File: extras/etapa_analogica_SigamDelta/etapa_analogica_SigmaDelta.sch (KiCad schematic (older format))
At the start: 20 parts, among them P1 CONN_02X10, P2 CONN_01X03, P3 CONN_02X10, P4 BNC

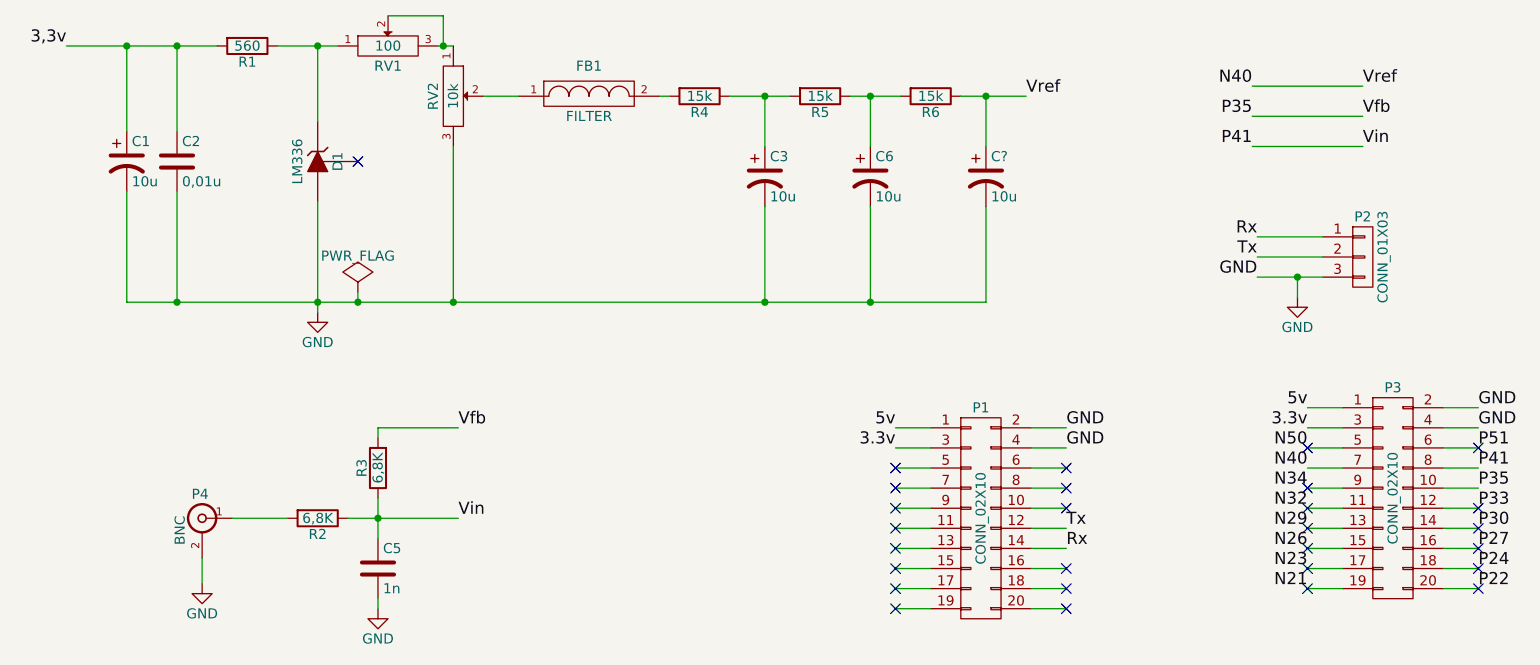
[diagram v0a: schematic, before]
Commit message: Agregado rooteo placa en Kicad
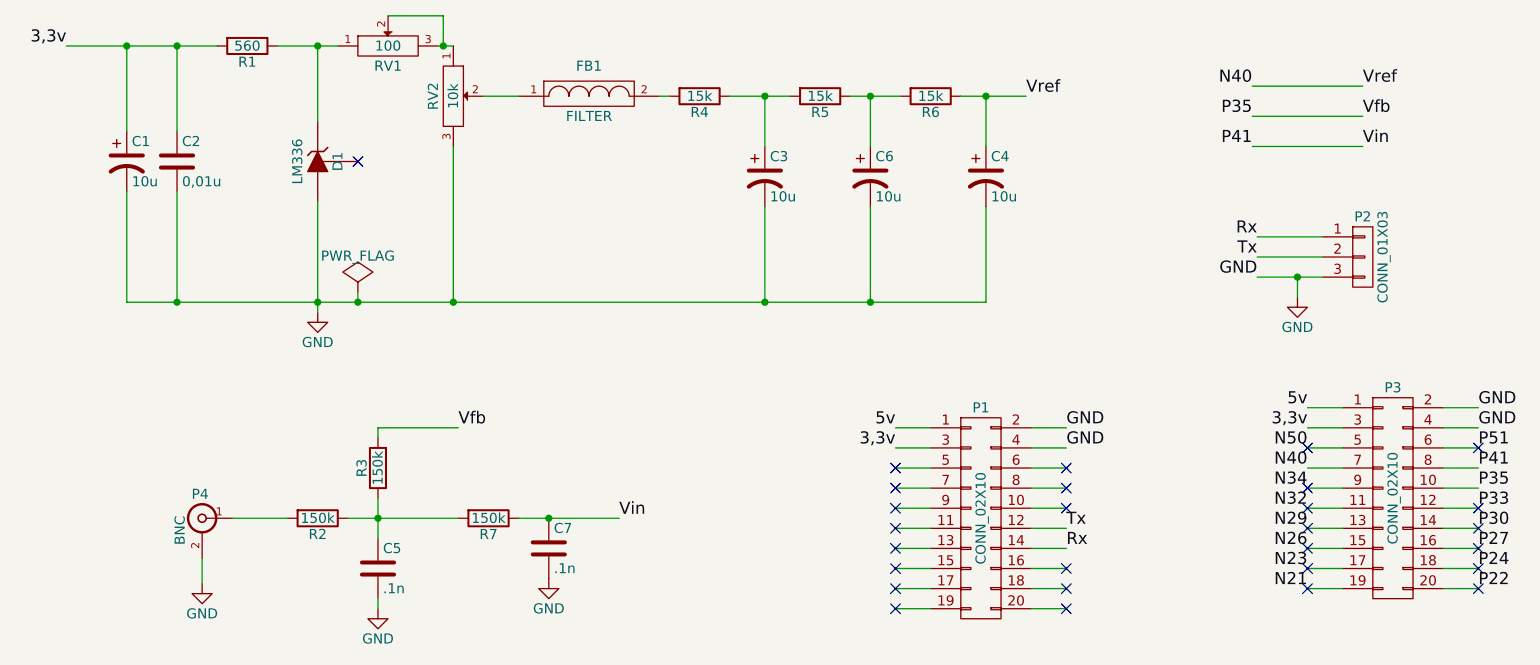
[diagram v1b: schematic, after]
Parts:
- added C7: .1n, Capacitors_SMD:C_0805, symbol C
- added R7: 150k, Resistors_SMD:R_0805_HandSoldering, symbol R
- C1: footprint Capacitors_SMD:c_elec_4x5.7 -> Capacitors_SMD:c_elec_4x4.5
- C5: value 1n -> .1n
- R2, R3: value 6,8K -> 150k
- gave numbers to parts that had none: 1
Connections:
- net 3.3v is gone; now on net 3,3v: P1.3 (P3), P3.3 (P3)
- net GND: now also C7.2
- net P41: now also C7.1, R7.1; no longer C5.1, R2.1, R3.1
- new net: C5.1, R2.1, R3.1, R7.2
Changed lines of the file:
@@
 P 3700 3600
 F 0 "R2" V 3780 3600 50  0000 C CNN
-F 1 "6,8K" V 3700 3600 50  0000 C CNN
+F 1 "150k" V 3700 3600 50  0000 C CNN
 F 2 "Resistors_SMD:R_0805_HandSoldering" V 3630 3600 30  0001 C CNN
 F 3 "" H 3700 3600 30  0000 C CNN
@@
 P 4000 3350
 F 0 "R3" V 4080 3350 50  0000 C CNN
-F 1 "6,8K" V 4000 3350 50  0000 C CNN
+F 1 "150k" V 4000 3350 50  0000 C CNN
 F 2 "Resistors_SMD:R_0805_HandSoldering" V 3930 3350 30  0001 C CNN
 F 3 "" H 4000 3350 30  0000 C CNN
@@
 P 4000 3850
 F 0 "C5" H 4025 3950 50  0000 L CNN
-F 1 "1n" H 4025 3750 50  0000 L CNN
+F 1 ".1n" H 4025 3750 50  0000 L CNN
 F 2 "Capacitors_SMD:C_0805" H 4038 3700 30  0001 C CNN
 F 3 "" H 4000 3850 60  0000 C CNN
@@
 F 0 "C1" H 2775 1925 50  0000 L CNN
 F 1 "10u" H 2775 1725 50  0000 L CNN
-F 2 "Capacitors_SMD:c_elec_4x5.7" H 2750 1825 60  0001 C CNN
+F 2 "Capacitors_SMD:c_elec_4x4.5" H 2750 1825 60  0001 C CNN
 F 3 "" H 2750 1825 60  0000 C CNN
 	1    2750 1825
@@
 5v
 Text Label 8625 3150 2    60   ~ 0
-3.3v
+3,3v
 Text Label 8625 3250 2    60   ~ 0
 N50
@@
 Text Label 4400 3150 0    60   ~ 0
 Vfb
-Text Label 4400 3600 0    60   ~ 0
+Text Label 5200 3600 0    60   ~ 0
 Vin
 Text Label 2450 1250 2    60   ~ 0
@@
 5v
 Text Label 6575 3250 2    60   ~ 0
-3.3v
+3,3v
 NoConn ~ 7425 3350
 NoConn ~ 6575 3350
@@
 NoConn ~ 3900 1825
 $Comp
-L CP1 C?
+L CP1 C4
 U 1 1 56200ADB
 P 7025 1900
-F 0 "C?" H 7050 2000 50  0000 L CNN
+F 0 "C4" H 7050 2000 50  0000 L CNN
 F 1 "10u" H 7050 1800 50  0000 L CNN
 F 2 "Capacitors_Tantalum_SMD:TantalC_SizeA_EIA-3216_HandSoldering" H 7025 1900 60  0001 C CNN
@@
 Wire Wire Line
 	7025 2050 7025 2525
+$Comp
+L R R7
+U 1 1 56257197
+P 4550 3600
+F 0 "R7" V 4630 3600 50  0000 C CNN
+F 1 "150k" V 4550 3600 50  0000 C CNN
+F 2 "Resistors_SMD:R_0805_HandSoldering" V 4480 3600 30  0001 C CNN
+F 3 "" H 4550 3600 30  0000 C CNN
+	1    4550 3600
+	0    1    1    0
+$EndComp
+$Comp
+L C C7
+U 1 1 56257208
+P 4850 3750
+F 0 "C7" H 4875 3850 50  0000 L CNN
+F 1 ".1n" H 4875 3650 50  0000 L CNN
+F 2 "Capacitors_SMD:C_0805" H 4888 3600 30  0001 C CNN
+F 3 "" H 4850 3750 60  0000 C CNN
+	1    4850 3750
+	1    0    0    -1
+$EndComp
+Wire Wire Line
+	4700 3600 5200 3600
+Connection ~ 4850 3600
+$Comp
+L GND #PWR06
+U 1 1 5625737A
+P 4850 3900
+F 0 "#PWR06" H 4850 3650 50  0001 C CNN
+F 1 "GND" H 4850 3750 50  0000 C CNN
+F 2 "" H 4850 3900 60  0000 C CNN
+F 3 "" H 4850 3900 60  0000 C CNN
+	1    4850 3900
+	1    0    0    -1
+$EndComp
 $EndSCHEMATC
